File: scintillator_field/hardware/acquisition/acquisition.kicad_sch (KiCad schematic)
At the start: 6 parts, among them J1 USB_C_16P_F, U10 USBLC6-2SC6

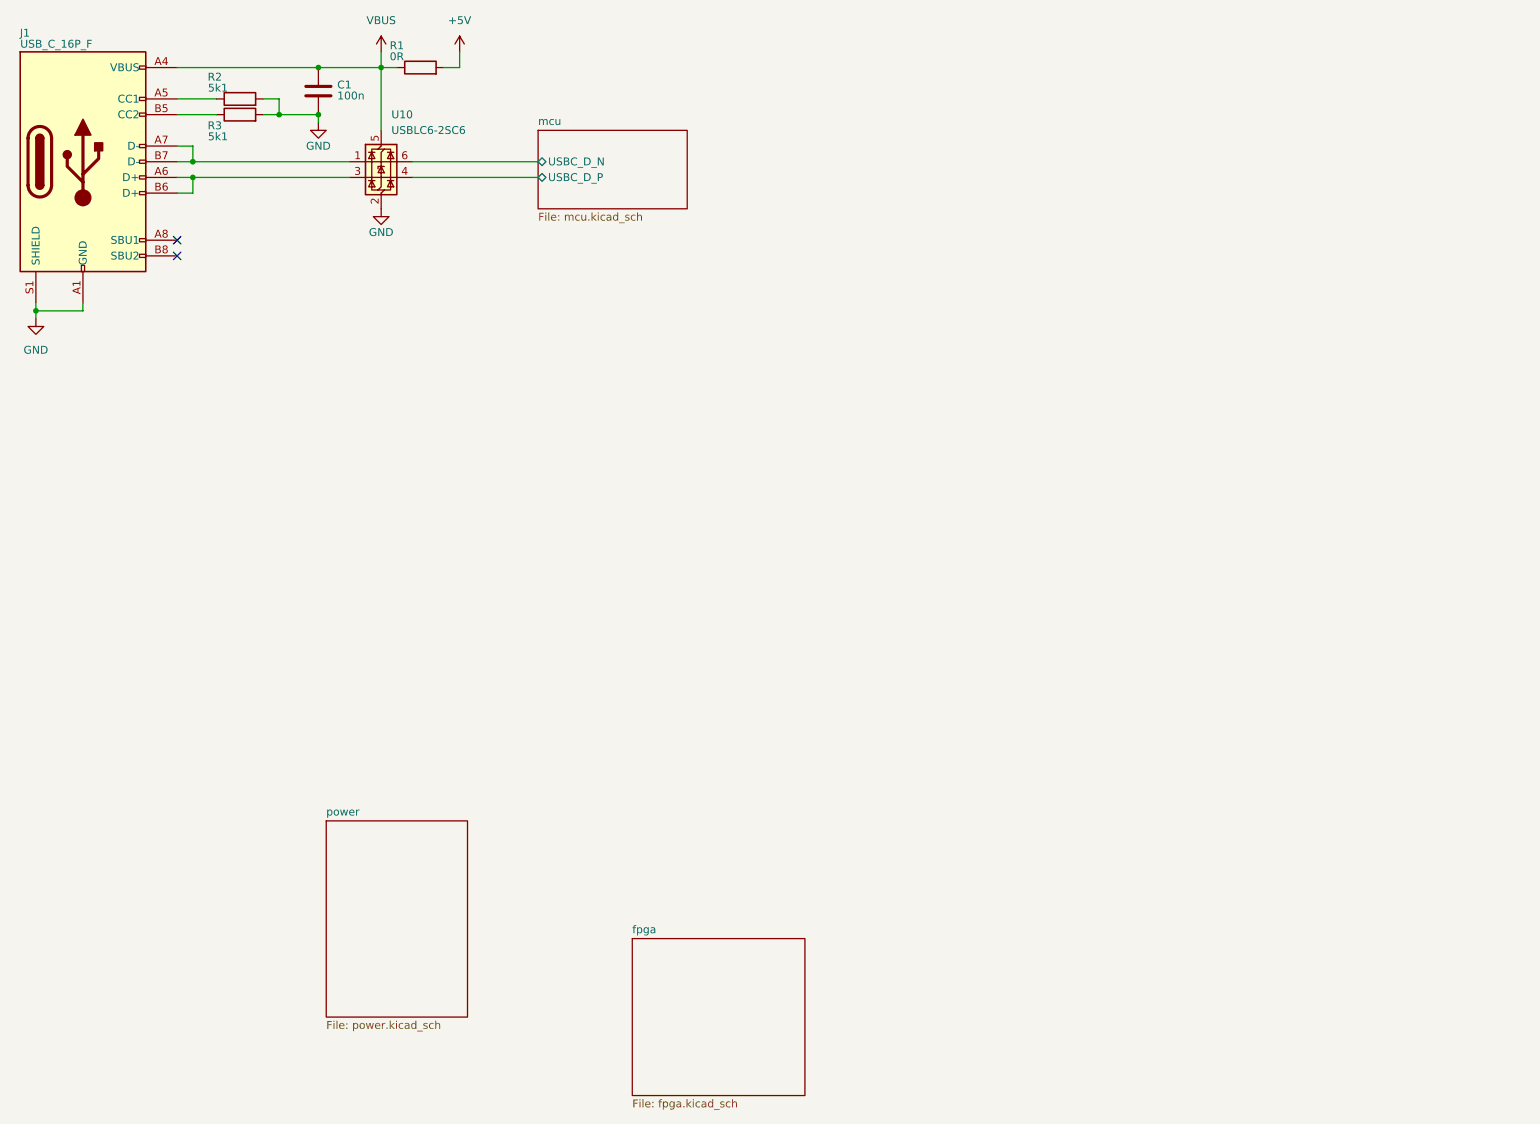
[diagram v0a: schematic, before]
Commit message: acquisition v2 basics
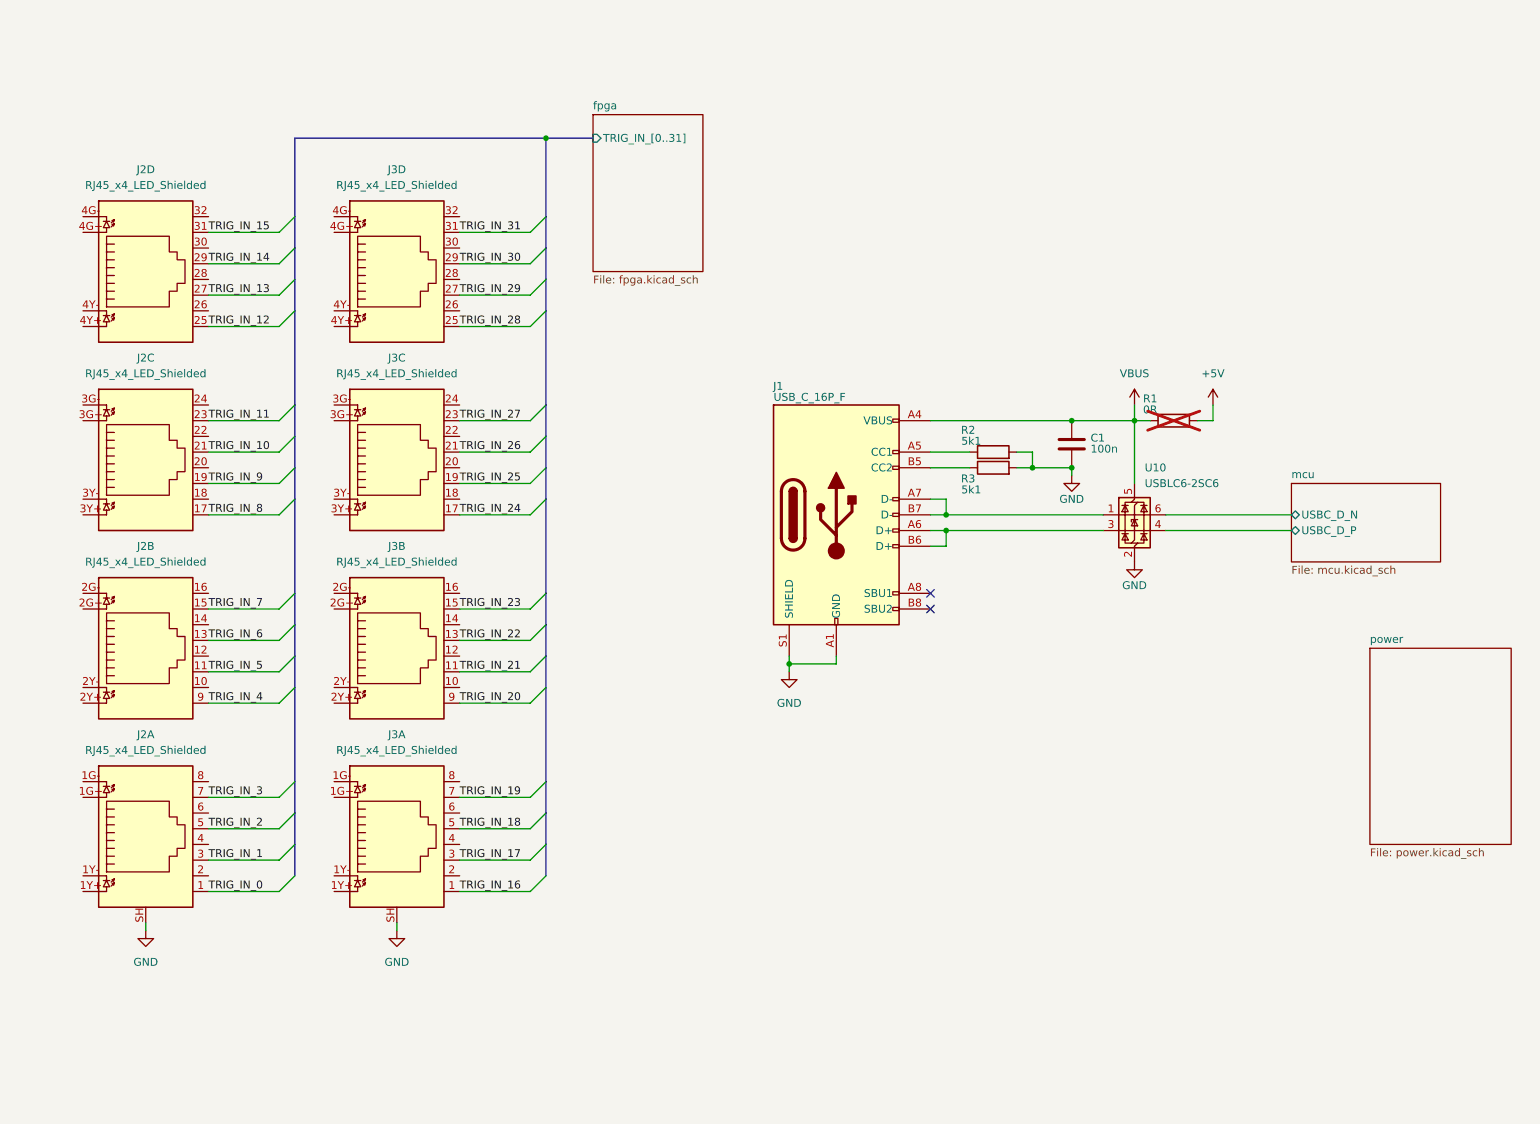
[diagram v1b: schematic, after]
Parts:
- added J2, J3: RJ45_x4_LED_Shielded, symbol rj45:RJ45_x4_LED_Shielded
- R1: now not fitted
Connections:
- net GND: now also J2.SH, J3.SH
- new net TRIG_IN_0: J2.1
- new net TRIG_IN_1: J2.3
- new net TRIG_IN_10: J2.21
- new net TRIG_IN_11: J2.23
- new net TRIG_IN_12: J2.25
- new net TRIG_IN_13: J2.27
- new net TRIG_IN_14: J2.29
- new net TRIG_IN_15: J2.31
- new net TRIG_IN_16: J3.1
- new net TRIG_IN_17: J3.3
- new net TRIG_IN_18: J3.5
- new net TRIG_IN_19: J3.7
- new net TRIG_IN_2: J2.5
- new net TRIG_IN_20: J3.9
- new net TRIG_IN_21: J3.11
- new net TRIG_IN_22: J3.13
- new net TRIG_IN_23: J3.15
- new net TRIG_IN_24: J3.17
- new net TRIG_IN_25: J3.19
- new net TRIG_IN_26: J3.21
- new net TRIG_IN_27: J3.23
- new net TRIG_IN_28: J3.25
- new net TRIG_IN_29: J3.27
- new net TRIG_IN_3: J2.7
- new net TRIG_IN_30: J3.29
- new net TRIG_IN_31: J3.31
- new net TRIG_IN_4: J2.9
- new net TRIG_IN_5: J2.11
- new net TRIG_IN_6: J2.13
- new net TRIG_IN_7: J2.15
- new net TRIG_IN_8: J2.17
- new net TRIG_IN_9: J2.19
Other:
- sheet fpga ports: added TRIG_IN_[0..31]; removed none
- moved on the sheet: C1, J1, R2, R3, U10
